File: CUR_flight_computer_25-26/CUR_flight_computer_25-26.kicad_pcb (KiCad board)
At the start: 4 copper layers, 53.2 x 117.5 mm, 143 parts, among them J1 3220-14-0100-00, J10 PYRO, J11 PYRO, J12 USB_C_Receptacle_USB2.0_16P, J13 Conn_01x04_Pin, J14 Conn_Coaxial_Small, J2 Screw_Terminal_01x02, J3 Screw_Terminal_01x02, J4 XT30PW-M, J5 XT30PW-M, J6 Micro_SD_Card, J7 Conn_01x02_Pin, J8 PYRO, J9 PYRO, Q1 NTR4003N, SW1 GSPTS0018, SW2 SW_SPDT, SW3 GSPTS0018, SW4 GSPTS0018, SW5 GSPTS0018, U1 STM32H523VETx, U10 W25Q32JVSS, U11 SAM-M8Q, U12 BUK9K25-40RAX, U13 BUK9K25-40RAX, U14 USBLC6-2SC6, U2 IIS2MDC, U3 LPS22HB, U4 LSM6DSV80X, U5 E22-400M30S, U6 BU33SD5, U7 LM66200, U8 ZXCT180A4W5, U9 ZXCT180A4W5, Y1 16M18PX/XT324-10/10

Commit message: Update CUR_flight_computer_25-26.kicad_pcb
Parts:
- added D3: ESDZV5HS-1BF4, Diode_SMD:D_0201_0603Metric, F.Cu at (82.7, 86.8)
- added D8: ESDZV5HS-1BF4, Diode_SMD:D_0201_0603Metric, F.Cu at (82.7, 88.5)
- moved U5 75.4 mm to (138.9, 116.7), turned to 0 degrees
- moved J1 7.09 mm to (86.1, 79.9), turned to 0 degrees
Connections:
- J13 pad e: /MCU/LCD_SDA -> (no net)

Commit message: ahhhh my eyes (decent layout)
put things on both sides
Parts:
- C10, C12, C13, C14, C15, C16, C17, C2, C25, C26, C27, C3, C4, C5, C6, C7, C9, FB1, R2, R7, R9, SW1, U1, U5, Y1: moved to B.Cu
- D17, Q1, R48, R49: moved to F.Cu
- J1: footprint Connector_CNC_Tech:CNC_Tech_3220-14-0100-00 -> Connector_CNC_Tech:CNC_Tech_3020-14-0300-00_CNC
- moved C25 107.6 mm to (54.1, 41.3), turned to 90 degrees
- moved U5 91.7 mm to (69.2, 57.0), turned to 180 degrees
- moved SW2 79.8 mm to (55.8, 113.5)
- moved R1 71.8 mm to (60.2, 108.2)
- moved R8 67.4 mm to (54.0, 48.2), turned to 90 degrees
- moved D13 65.7 mm to (56.2, 60.6), turned to 90 degrees
- moved J4 59.3 mm to (117.8, 32.5), turned to 0 degrees
- moved R55 55.8 mm to (73.2, 73.0), turned to 0 degrees
- moved R56 55.8 mm to (73.2, 78.5), turned to 0 degrees
- moved R52 55.3 mm to (64.5, 75.7), turned to -90 degrees
- moved LED_2 54.3 mm to (73.5, 75.8)
- moved R54 53.7 mm to (76.5, 75.8), turned to -90 degrees
- moved C31 53.2 mm to (62.6, 84.4)
- moved C32 53.1 mm to (64.2, 84.3)
- moved D12 52.6 mm to (63.8, 88.6)
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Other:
- board size 53.2 x 117.5 mm -> 48.2 x 87.2 mm

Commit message: Update CUR_flight_computer_25-26.kicad_pcb
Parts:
- moved J5 79.3 mm to (55.0, 44.1)
- moved J4 31.4 mm to (88.6, 44.1)
- moved R7 9.79 mm to (84.1, 59.4)
- moved C30 9.66 mm to (73.9, 93.3), turned to 0 degrees
- moved R22 8.65 mm to (78.4, 87.7), turned to 135 degrees
- moved R21 8.61 mm to (77.3, 88.8), turned to 135 degrees
- moved R25 8.35 mm to (76.2, 89.9), turned to 135 degrees
- moved R27 7.47 mm to (73.9, 91.7), turned to 0 degrees
- moved D17 5.38 mm to (65.1, 101.3)
- moved Q1 5.38 mm to (62.0, 97.9)
- moved R49 5.38 mm to (63.6, 97.9)
- moved R48 5.10 mm to (65.5, 97.8)
- moved D4 4.94 mm to (56.7, 50.9)
- moved D6 4.94 mm to (57.3, 50.4)
- moved R10 4.94 mm to (64.0, 52.1)
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
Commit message: routing updates
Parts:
- J12: footprint SAMESKY_UJ20-C-H-G-SMT-P16-TR:SAMESKY_UJ20-C-H-G-SMT-P16-TR -> SAMESKY_UJ20-C-H-G-SMT-5-P16-TR:SAMESKY_UJ20-C-H-G-SMT-5-P16-TR
- J4, J5: footprint Connector_AMASS_XT:AMASS_XT30PW-M_1x02_P2.50mm_Horizontal -> Connector_AMASS:AMASS_XT30U-M_1x02_P5.0mm_Vertical
- moved J4 36.1 mm to (52.5, 43.4), turned to 180 degrees
- moved J5 30.0 mm to (85.0, 43.2)
- moved J1 4.94 mm to (125.1, 64.6)
- moved J12 3.96 mm to (68.5, 35.6)
- moved C25 1.68 mm to (54.0, 46.5)
- moved R8 1.58 mm to (54.0, 49.8)
- moved J11 0.97 mm to (49.8, 69.8)
- moved J9 0.82 mm to (49.8, 59.8)
- moved J2 0.73 mm to (49.9, 49.8)
- moved J8 0.70 mm to (87.6, 74.5)
- moved U5 0.35 mm to (69.1, 58.8)
- moved J10 0.35 mm to (87.6, 64.5)
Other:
- board size 48.2 x 87.2 mm -> 48.8 x 84.8 mm

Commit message: routing updates
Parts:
- J10, J11, J2, J3, J8, J9: footprint TerminalBlock_Phoenix:TerminalBlock_Phoenix_PT-1,5-2-5.0-H_1x02_P5.00mm_Horizontal -> Terminal_SAMESKY_TB0011-350-02GR:SAMESKY_TB0011-350-02GR
- moved J2 10.6 mm to (51.0, 60.2)
- moved J9 7.60 mm to (51.0, 67.2)
- moved J3 5.58 mm to (86.5, 60.0)
- moved J11 4.67 mm to (51.0, 74.2)
- moved J4 4.65 mm to (51.0, 47.8), turned to -90 degrees
- moved J5 4.60 mm to (86.8, 47.5), turned to -90 degrees
- moved Q1 4.25 mm to (65.9, 99.5)
- moved R49 4.25 mm to (67.5, 99.5)
- moved R48 4.25 mm to (69.4, 99.4)
- moved J12 3.81 mm to (70.1, 39.1)
- moved J7 3.79 mm to (81.2, 84.0)
- moved R50 3.35 mm to (73.2, 109.8), turned to 135 degrees
- moved J10 2.73 mm to (86.5, 67.0)
- moved SW2 2.55 mm to (59.5, 113.5)
- moved C5 2.52 mm to (48.0, 90.8)
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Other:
- board size 48.8 x 84.8 mm -> 45.2 x 81 mm

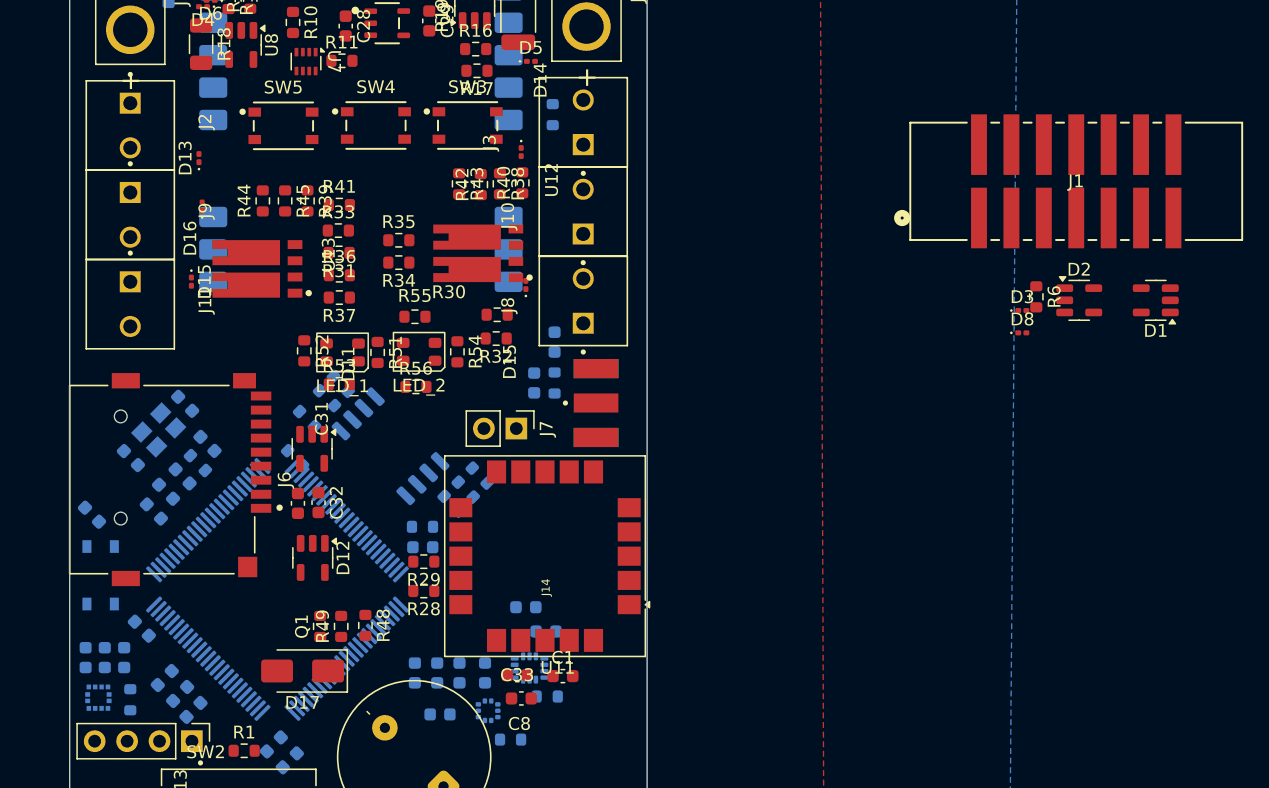
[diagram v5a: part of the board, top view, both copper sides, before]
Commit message: added in debug header to layout
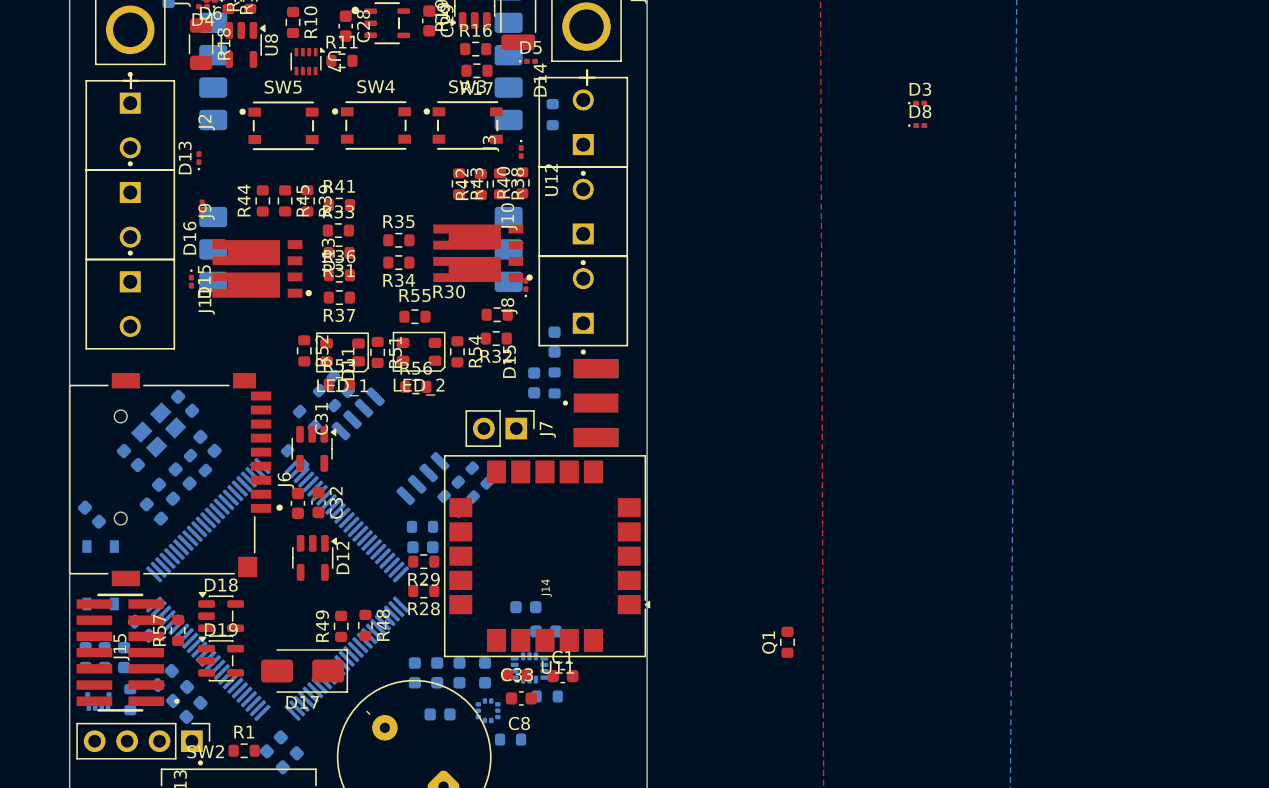
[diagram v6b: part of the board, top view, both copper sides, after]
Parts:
- removed D1, D2: ESDA5V3SC5, Package_TO_SOT_SMD:SOT-23-5
- removed J1: 3220-14-0100-00, Connector_CNC_Tech:CNC_Tech_3020-14-0300-00_CNC
- removed R6: 150, Resistor_SMD:R_0603_1608Metric
- added D18: ESDA5V3SC5, Package_TO_SOT_SMD:SOT-23-5, F.Cu at (58.1, 98.7)
- added D19: ESDA5V3SC5, Package_TO_SOT_SMD:SOT-23-5, F.Cu at (58.1, 102.2)
- added J15: FTSH-107-01-X-DV-K-TR, Connector_SAMTEC_FTSH-107-01-X-DV-K-TR:SAMTEC_FTSH-107-01-X-DV-K-TR, F.Cu at (50.2, 101.6)
- added R57: 150, Resistor_SMD:R_0603_1608Metric, F.Cu at (54.8, 99.8)
- moved Q1 36.6 mm to (102.5, 100.8)
- moved D3 18.1 mm to (112.9, 58.5)
- moved D8 18.1 mm to (112.9, 60.2)

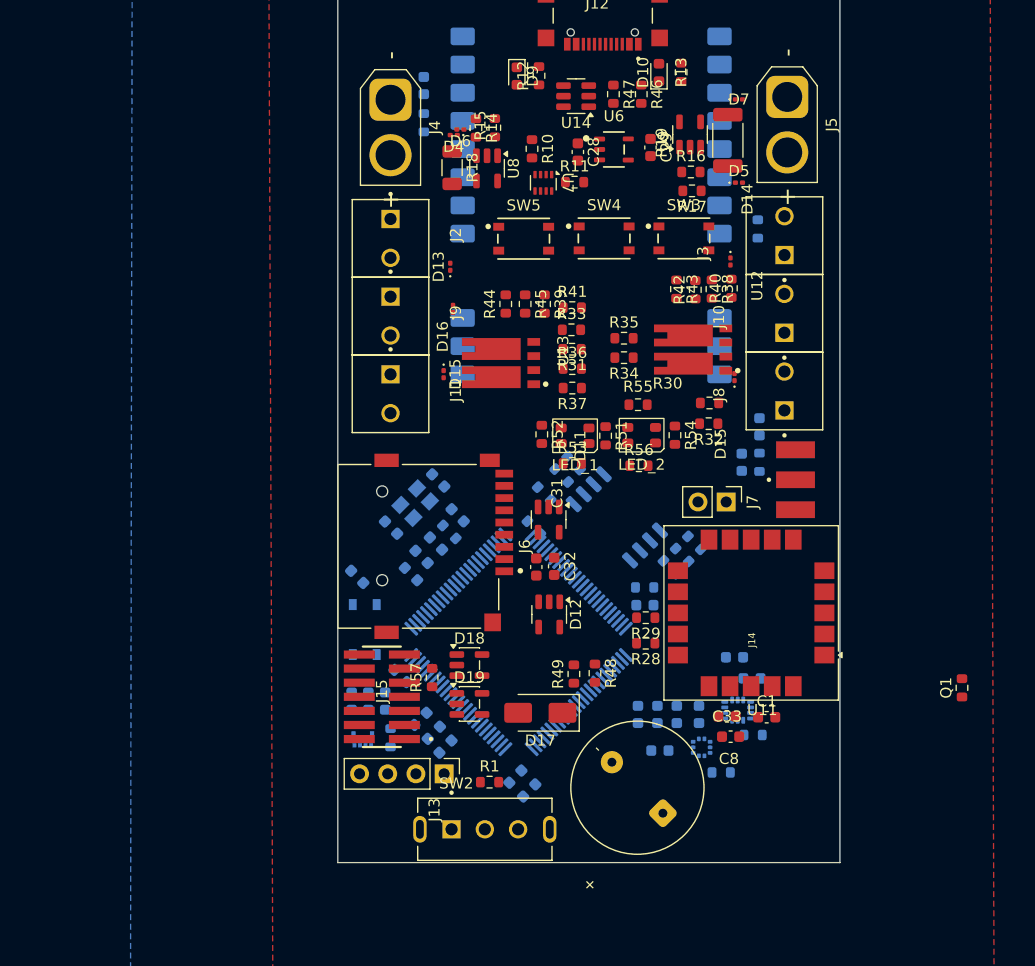
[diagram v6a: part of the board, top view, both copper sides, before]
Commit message: added testpoints to schematic
need to update layout
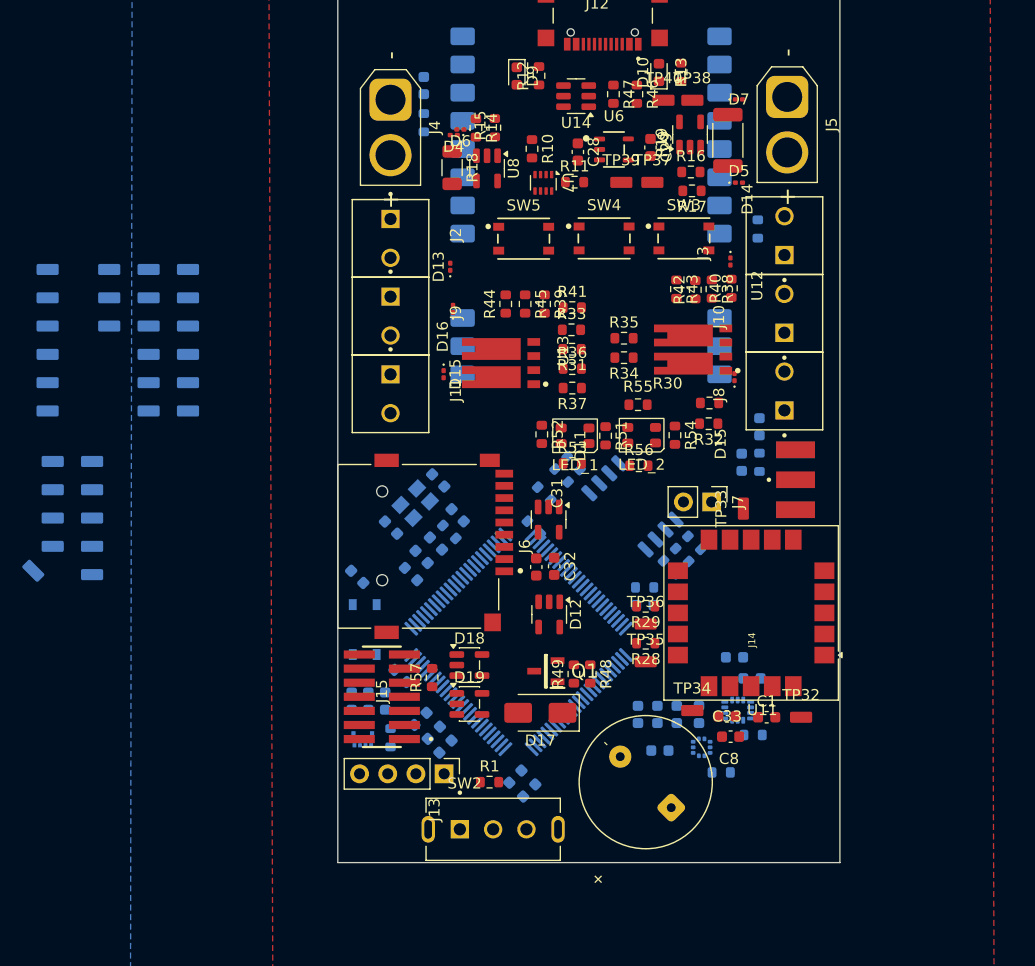
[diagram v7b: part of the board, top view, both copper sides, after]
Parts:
- added TP1: TestPoint_Small, TestPoint_KOASpeer:TestPoint_Chip_RCUCTE_0603, B.Cu at (32.8, 63.0)
- added TP10: TestPoint_Small, TestPoint_KOASpeer:TestPoint_Chip_RCUCTE_0603, B.Cu at (29.2, 70.7)
- added TP11: TestPoint_Small, TestPoint_KOASpeer:TestPoint_Chip_RCUCTE_0603, B.Cu at (29.2, 73.2)
- added TP12: TestPoint_Small, TestPoint_KOASpeer:TestPoint_Chip_RCUCTE_0603, B.Cu at (29.2, 75.8)
- added TP13: TestPoint_Small, TestPoint_KOASpeer:TestPoint_Chip_RCUCTE_0603, B.Cu at (25.6, 63.0)
- added TP14: TestPoint_Small, TestPoint_KOASpeer:TestPoint_Chip_RCUCTE_0603, B.Cu at (25.6, 65.6)
- added TP15: TestPoint_Small, TestPoint_KOASpeer:TestPoint_Chip_RCUCTE_0603, B.Cu at (25.6, 68.2)
- added TP16: TestPoint_Small, TestPoint_KOASpeer:TestPoint_Chip_RCUCTE_0603, B.Cu at (20.1, 63.0)
- added TP17: TestPoint_Small, TestPoint_KOASpeer:TestPoint_Chip_RCUCTE_0603, B.Cu at (20.1, 65.6)
- added TP18: TestPoint_Small, TestPoint_KOASpeer:TestPoint_Chip_RCUCTE_0603, B.Cu at (20.1, 68.2)
- added TP19: TestPoint_Small, TestPoint_KOASpeer:TestPoint_Chip_RCUCTE_0603, B.Cu at (20.1, 70.7)
- added TP2: TestPoint_Small, TestPoint_KOASpeer:TestPoint_Chip_RCUCTE_0603, B.Cu at (32.8, 65.6)
- added TP20: TestPoint_Small, TestPoint_KOASpeer:TestPoint_Chip_RCUCTE_0603, B.Cu at (20.1, 73.2)
- added TP21: TestPoint_Small, TestPoint_KOASpeer:TestPoint_Chip_RCUCTE_0603, B.Cu at (20.1, 75.8)
- added TP22: TestPoint_Small, TestPoint_KOASpeer:TestPoint_Chip_RCUCTE_0603, B.Cu at (24.1, 80.3)
- added TP23: TestPoint_Small, TestPoint_KOASpeer:TestPoint_Chip_RCUCTE_0603, B.Cu at (24.1, 82.9)
- added TP24: TestPoint_Small, TestPoint_KOASpeer:TestPoint_Chip_RCUCTE_0603, B.Cu at (24.1, 85.5)
- added TP25: TestPoint_Small, TestPoint_KOASpeer:TestPoint_Chip_RCUCTE_0603, B.Cu at (24.1, 88.0)
- added TP26: TestPoint_Small, TestPoint_KOASpeer:TestPoint_Chip_RCUCTE_0603, B.Cu at (24.1, 90.5)
- added TP27: TestPoint_Small, TestPoint_KOASpeer:TestPoint_Chip_RCUCTE_0603, B.Cu at (20.6, 80.3)
- added TP28: TestPoint_Small, TestPoint_KOASpeer:TestPoint_Chip_RCUCTE_0603, B.Cu at (20.6, 82.9)
- added TP29: TestPoint_Small, TestPoint_KOASpeer:TestPoint_Chip_RCUCTE_0603, B.Cu at (20.6, 85.5)
- added TP3: TestPoint_Small, TestPoint_KOASpeer:TestPoint_Chip_RCUCTE_0603, B.Cu at (32.8, 68.2)
- added TP30: TestPoint_Small, TestPoint_KOASpeer:TestPoint_Chip_RCUCTE_0603, B.Cu at (20.6, 88.0)
- added TP31: TestPoint_Small, TestPoint_KOASpeer:TestPoint_Chip_RCUCTE_0603, B.Cu at (18.8, 90.2)
- added TP32: TestPoint_Small, TestPoint_KOASpeer:TestPoint_Chip_RCUCTE_0603, F.Cu at (88.0, 103.4)
- added TP33: TestPoint_Small, TestPoint_KOASpeer:TestPoint_Chip_RCUCTE_0603, F.Cu at (82.8, 84.6)
- added TP34: TestPoint_Small, TestPoint_KOASpeer:TestPoint_Chip_RCUCTE_0603, F.Cu at (78.2, 102.8)
- added TP35: TestPoint_Small, TestPoint_KOASpeer:TestPoint_Chip_RCUCTE_0603, F.Cu at (74.0, 98.4)
- added TP36: TestPoint_Small, TestPoint_KOASpeer:TestPoint_Chip_RCUCTE_0603, F.Cu at (74.0, 95.0)
- added TP37: TestPoint, TestPoint_KOASpeer:TestPoint_Chip_RCUCTE_0603, F.Cu at (74.6, 55.2)
- added TP38: TestPoint, TestPoint_KOASpeer:TestPoint_Chip_RCUCTE_0603, F.Cu at (78.2, 47.8)
- added TP39: TestPoint, TestPoint_KOASpeer:TestPoint_Chip_RCUCTE_0603, F.Cu at (71.8, 55.2)
- added TP4: TestPoint_Small, TestPoint_KOASpeer:TestPoint_Chip_RCUCTE_0603, B.Cu at (32.8, 70.7)
- added TP40: TestPoint, TestPoint_KOASpeer:TestPoint_Chip_RCUCTE_0603, F.Cu at (75.6, 47.8)
- added TP5: TestPoint_Small, TestPoint_KOASpeer:TestPoint_Chip_RCUCTE_0603, B.Cu at (32.8, 73.2)
- added TP6: TestPoint_Small, TestPoint_KOASpeer:TestPoint_Chip_RCUCTE_0603, B.Cu at (32.8, 75.8)
- added TP7: TestPoint_Small, TestPoint_KOASpeer:TestPoint_Chip_RCUCTE_0603, B.Cu at (29.2, 63.0)
- added TP8: TestPoint_Small, TestPoint_KOASpeer:TestPoint_Chip_RCUCTE_0603, B.Cu at (29.2, 65.6)
- added TP9: TestPoint_Small, TestPoint_KOASpeer:TestPoint_Chip_RCUCTE_0603, B.Cu at (29.2, 68.2)
- Q1: footprint Resistor_SMD:R_0603_1608Metric -> NTR4003NT1G:SOT96P237X111-3N
- moved Q1 37.5 mm to (65.0, 99.2), turned to 180 degrees
- moved U10 1.71 mm to (72.8, 84.4)
- moved J7 1.31 mm to (79.9, 84.0)
- moved R29 1.03 mm to (74.0, 93.4)
- moved R50 0.90 mm to (74.0, 109.2)
- moved SW2 0.75 mm to (60.2, 113.5)
- moved R48 0.43 mm to (69.0, 99.5)
- moved R46 0.40 mm to (73.2, 47.3)

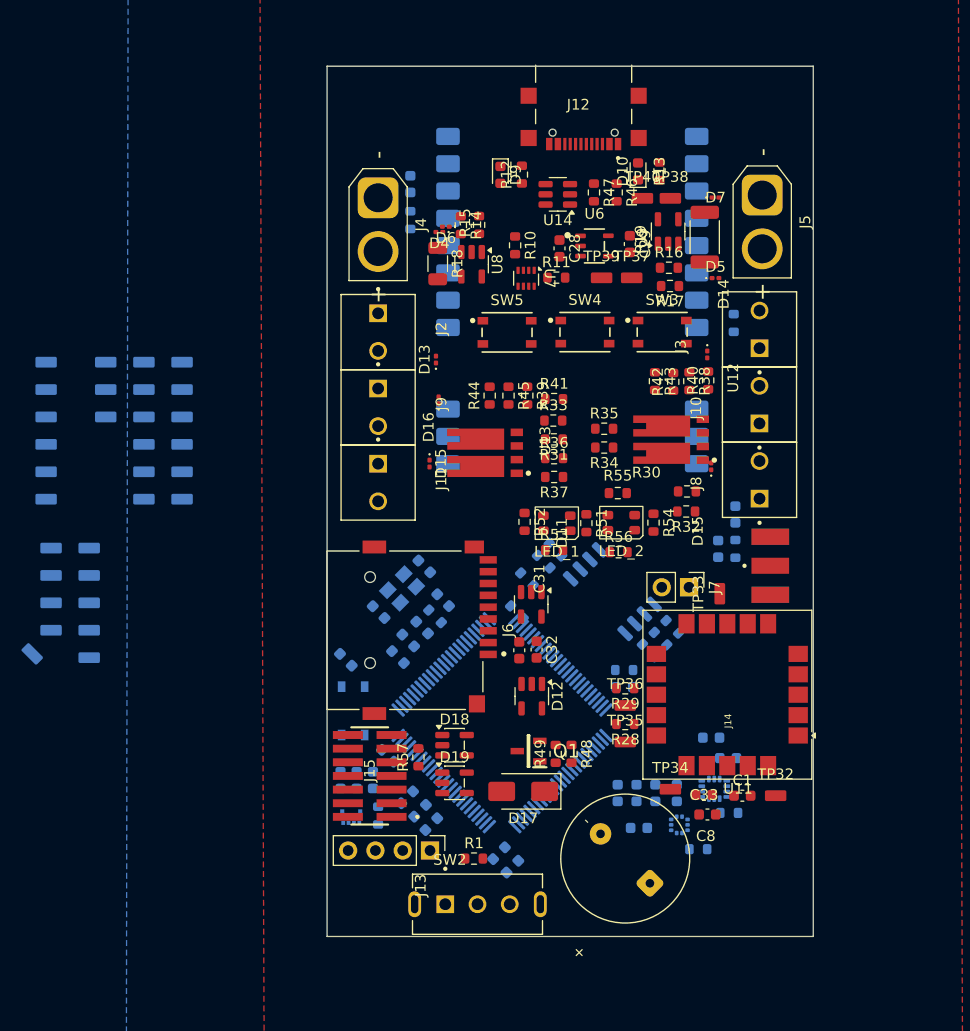
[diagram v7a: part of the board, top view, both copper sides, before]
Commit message: added testpoints
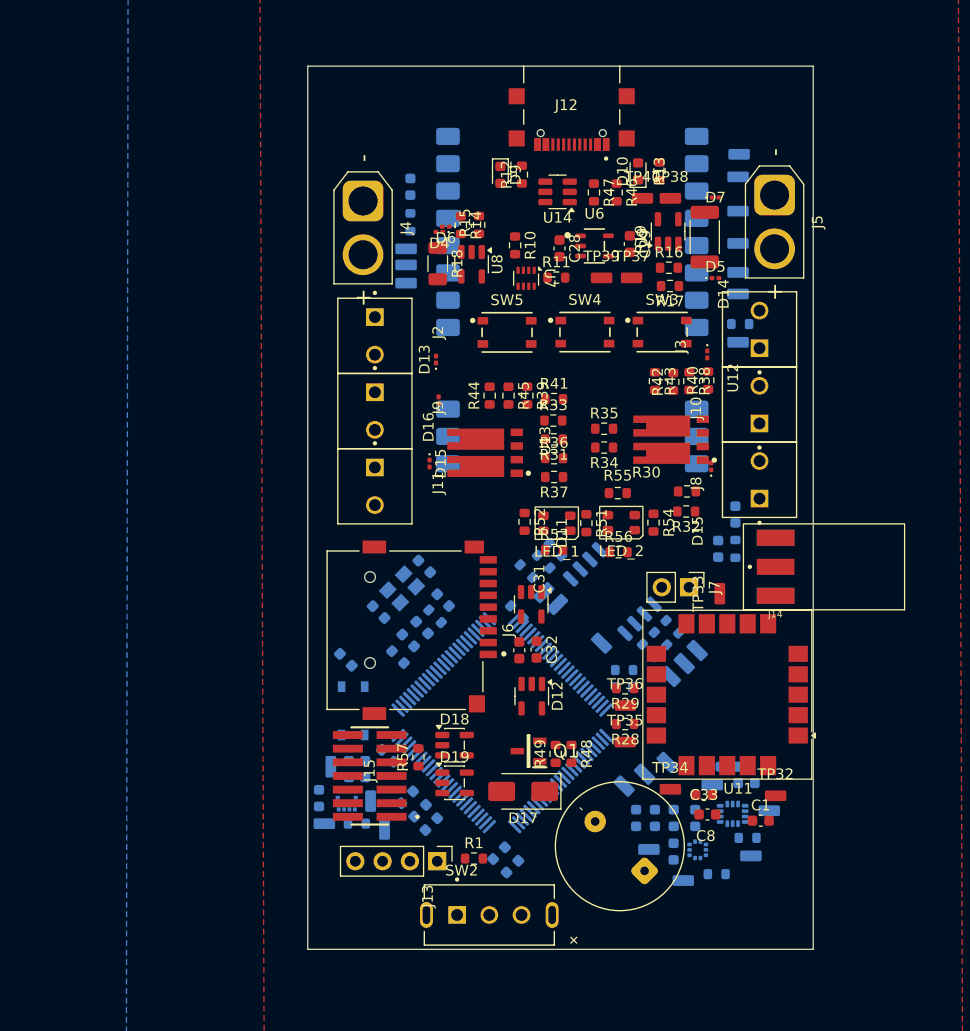
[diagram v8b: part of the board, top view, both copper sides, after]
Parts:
- removed TP7, TP8, TP9: TestPoint_Small, TestPoint_KOASpeer:TestPoint_Chip_RCUCTE_0603
- moved TP30 77.9 mm to (84.6, 43.7), turned to 0 degrees
- moved TP22 69.6 mm to (84.5, 45.8), turned to 0 degrees
- moved TP23 69.3 mm to (84.5, 49.0), turned to 0 degrees
- moved TP26 69.2 mm to (84.5, 56.7), turned to 0 degrees
- moved TP24 69.0 mm to (84.5, 52.0), turned to 0 degrees
- moved TP25 69.0 mm to (84.5, 54.7), turned to 0 degrees
- moved TP27 66.7 mm to (84.5, 61.2), turned to 0 degrees
- moved TP11 66.2 mm to (87.4, 104.8)
- moved TP16 65.7 mm to (79.5, 91.1), turned to 135 degrees
- moved TP17 65.3 mm to (80.7, 89.9), turned to 135 degrees
- moved TP6 62.5 mm to (85.7, 109.0)
- moved TP4 61.8 mm to (79.4, 111.3)
- moved TP10 61.7 mm to (82.1, 102.4)
- moved TP20 61.1 mm to (78.2, 92.3), turned to 135 degrees
- moved TP1 57.0 mm to (73.9, 102.5), turned to 135 degrees
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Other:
- board size 45.2 x 81 mm -> 47 x 82.2 mm
